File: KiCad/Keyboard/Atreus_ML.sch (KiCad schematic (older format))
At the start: 85 parts, among them K1 CHERRY_ML, K10 CHERRY_ML, K11 CHERRY_ML, K12 CHERRY_ML, K13 CHERRY_ML, K14 CHERRY_ML, K15 CHERRY_ML, K16 CHERRY_ML, K17 CHERRY_ML, K18 CHERRY_ML, K19 CHERRY_ML, K2 CHERRY_ML, K20 CHERRY_ML, K21 CHERRY_ML, K22 CHERRY_ML, K23 CHERRY_ML, K24 CHERRY_ML, K25 CHERRY_ML, K26 CHERRY_ML, K27 CHERRY_ML, K28 CHERRY_ML, K29 CHERRY_ML, K3 CHERRY_ML, K30 CHERRY_ML, K31 CHERRY_ML, K32 CHERRY_ML, K33 CHERRY_ML, K34 CHERRY_ML, K35 CHERRY_ML, K36 CHERRY_ML, K37 CHERRY_ML, K38 CHERRY_ML, K39 CHERRY_ML, K4 CHERRY_ML, K40 CHERRY_ML, K41 CHERRY_ML, K42 CHERRY_ML, K5 CHERRY_ML, K6 CHERRY_ML, K7 CHERRY_ML, K8 CHERRY_ML, K9 CHERRY_ML, U1 TEENSY2.0-Compact

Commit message: Rev one is done!
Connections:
- net at D1.2 (out), D2.2 (out), D3.2 (out)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: now also U1.6 (PF6); no longer U1.2 (PF0)
- net at D5.2 (out), D6.2 (out), D7.2 (out)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: now also U1.5 (PF5); no longer U1.3 (PF1)
- net at D13.2 (out), D14.2 (out), D15.2 (out)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: now also U1.3 (PF1); no longer U1.5 (PF5)
- net at D17.2 (out), D18.2 (out), D19.2 (out)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: now also U1.2 (PF0); no longer U1.6 (PF6)
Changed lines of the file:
@@
 	1    0    0    -1
 $EndComp
+NoConn ~ 9400 7350
+NoConn ~ 9600 7350
 Wire Wire Line
 	7550 7350 9200 7350
@@
 	8950 1750 8950 3100
 Wire Wire Line
-	7550 2150 7550 1750
-Wire Wire Line
-	6600 2150 7550 2150
-Wire Wire Line
-	7650 2100 7650 1750
-Wire Wire Line
-	6650 2100 7650 2100
-Wire Wire Line
-	7750 2050 7750 1750
+	6600 2150 7950 2150
+Wire Wire Line
+	6650 2100 7850 2100
 Wire Wire Line
 	6700 2050 7750 2050
 Wire Wire Line
-	7850 2000 7850 1750
-Wire Wire Line
-	6750 2000 7850 2000
-Wire Wire Line
-	7950 1950 7950 1750
-Wire Wire Line
-	6800 1950 7950 1950
-Wire Wire Line
 	9350 2100 9350 1750
 Wire Wire Line
 	10850 2100 9350 2100
 Wire Wire Line
-	9750 2000 9750 1750
-Wire Wire Line
-	10800 2000 9750 2000
-Wire Wire Line
-	9850 1950 9850 1750
-Wire Wire Line
-	10750 1950 9850 1950
-Wire Wire Line
-	9950 1900 9950 1750
-Wire Wire Line
-	10700 1900 9950 1900
-Wire Wire Line
-	10050 1850 10050 1750
-Wire Wire Line
-	10650 1850 10050 1850
-Wire Wire Line
-	11500 10000 11500 9450
-Wire Wire Line
 	9400 10000 11500 10000
 Wire Wire Line
@@
 	11300 1100 11150 1100
 Wire Wire Line
-	10650 750  10650 1850
-Wire Wire Line
-	15000 750  10650 750
-Wire Wire Line
-	10700 800  10700 1900
-Wire Wire Line
-	14100 800  10700 800
-Wire Wire Line
-	10750 850  10750 1950
-Wire Wire Line
-	13200 850  10750 850
-Wire Wire Line
-	10800 900  10800 2000
-Wire Wire Line
-	12300 900  10800 900
+	10650 1850 10650 750
+Wire Wire Line
+	10650 750  15000 750
+Wire Wire Line
+	10700 1900 10700 800
+Wire Wire Line
+	10700 800  14100 800
+Wire Wire Line
+	10750 1950 10750 850
+Wire Wire Line
+	10750 850  13200 850
+Wire Wire Line
+	10800 2000 10800 900
+Wire Wire Line
+	10800 900  12300 900
 Wire Wire Line
 	10850 950  10850 2100
@@
 	8650 5500 8650 7350
 Connection ~ 8650 7350
-NoConn ~ 9400 7350
-NoConn ~ 9600 7350
+Wire Wire Line
+	7950 2150 7950 1750
+Wire Wire Line
+	7850 2100 7850 1750
+Wire Wire Line
+	7750 2050 7750 1750
+Wire Wire Line
+	6750 2000 7650 2000
+Wire Wire Line
+	7650 2000 7650 1750
+Wire Wire Line
+	6800 1950 7550 1950
+Wire Wire Line
+	7550 1950 7550 1750
+Wire Wire Line
+	11500 10000 11500 9700
+Wire Wire Line
+	11500 9700 11450 9700
+Wire Wire Line
+	11450 9700 11450 9450
+Connection ~ 11450 9450
+Wire Wire Line
+	9850 1950 10750 1950
+Wire Wire Line
+	9750 2000 10800 2000
+Wire Wire Line
+	9750 1750 9750 2000
+Wire Wire Line
+	9850 1950 9850 1750
+Wire Wire Line
+	10050 1750 10050 1850
+Wire Wire Line
+	10050 1850 10650 1850
+Wire Wire Line
+	10700 1900 9950 1900
+Wire Wire Line
+	9950 1900 9950 1750
 $EndSCHEMATC

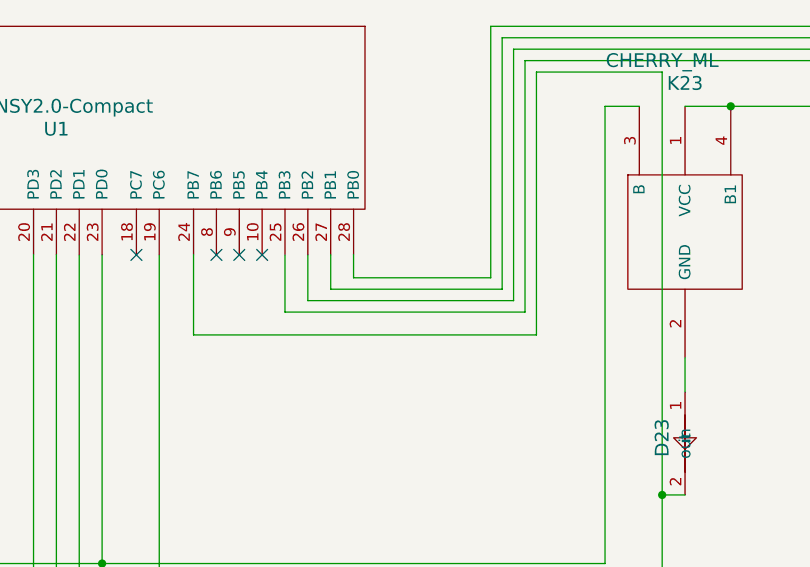
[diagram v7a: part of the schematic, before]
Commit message: Starting rev 2, cleaning up columns
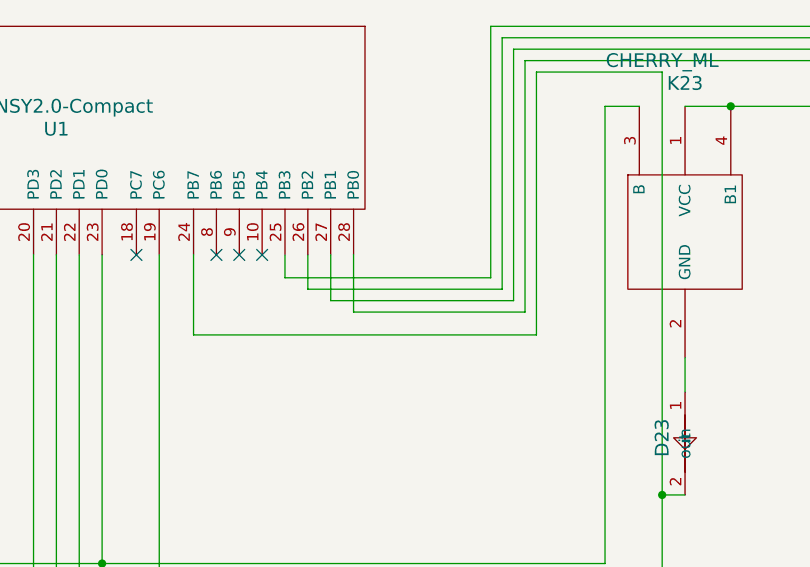
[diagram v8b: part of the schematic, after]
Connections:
- net at D27.2 (out), D28.2 (out), D29.2 (out)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: now also U1.28 (PB0); no longer U1.25 (PB3)
- net at D31.2 (out), D32.2 (out), D33.2 (out)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: now also U1.27 (PB1); no longer U1.26 (PB2)
- net at D35.2 (out), D36.2 (out), D37.2 (out)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: now also U1.26 (PB2); no longer U1.27 (PB1)
- net at D39.2 (out), D40.2 (out), D41.2 (out)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: now also U1.25 (PB3); no longer U1.28 (PB0)
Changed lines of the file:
@@
 Connection ~ 11450 9450
 Wire Wire Line
-	9850 1950 10750 1950
+	9750 1850 10650 1850
 Wire Wire Line
-	9750 2000 10800 2000
+	9850 1900 10700 1900
 Wire Wire Line
-	9750 1750 9750 2000
+	9750 1850 9750 1750
 Wire Wire Line
-	9850 1950 9850 1750
+	9850 1900 9850 1750
 Wire Wire Line
-	10050 1750 10050 1850
+	10750 1950 9950 1950
 Wire Wire Line
-	10050 1850 10650 1850
+	9950 1950 9950 1750
 Wire Wire Line
-	10700 1900 9950 1900
+	10800 2000 10050 2000
 Wire Wire Line
-	9950 1900 9950 1750
+	10050 2000 10050 1750
 $EndSCHEMATC
